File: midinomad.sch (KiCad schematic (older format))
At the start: 47 parts, among them U1 6N138

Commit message: Updated schematics. Still work in progress.
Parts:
- removed D2, D3: 1N4148, Diode_THT:D_DO-35_SOD27_P7.62mm_Horizontal, symbol Diode:1N4148
- removed R4: 4k7, symbol Device:R
- removed R5: 470R, symbol Device:R
- removed R6: 10k, symbol Device:R
- removed R7: 8k2, symbol Device:R
- removed R8: 300R, symbol Device:R
- added C1: 0.33uF, symbol pspice:C
- added C2: 0.1uF, symbol pspice:C
- added J2: MIDI OUT, w_conn_av:din-5, symbol Connector:DIN-5_180degree
- added J5: Conn_01x10_Female, symbol Connector:Conn_01x10_Female
- added J6: Conn_01x10_Male, symbol Connector:Conn_01x10_Male
- added J7: Jack-DC, symbol Connector:Jack-DC
- added JP2: Jumper, Connector_PinHeader_2.54mm:PinHeader_1x02_P2.54mm_Vertical, symbol Device:Jumper
- added R16: 9k1, Resistor_THT:R_Axial_DIN0207_L6.3mm_D2.5mm_P10.16mm_Horizontal, symbol Device:R
- added R17: 5k6, Resistor_THT:R_Axial_DIN0207_L6.3mm_D2.5mm_P10.16mm_Horizontal, symbol Device:R
- added R18: 2k7, Resistor_THT:R_Axial_DIN0207_L6.3mm_D2.5mm_P10.16mm_Horizontal, symbol Device:R
- added R25: 220R, Resistor_THT:R_Axial_DIN0207_L6.3mm_D2.5mm_P10.16mm_Horizontal, symbol Device:R
- added U2: L7805, symbol Regulator_Linear:L7805
- D2, D3, D4, D5, D6, D7: renamed from D?; footprint (none) -> LED_THT:LED_D5.0mm
- J1: renamed from J?; value DIN-5_180degree -> MIDI IN; footprint (none) -> w_conn_av:din-5
- J3: renamed from J?; footprint (none) -> w_conn_av:din-5; Note (none) -> Nomad 45, 55
- J4: renamed from J?; footprint (none) -> Connector_PinHeader_2.54mm:PinHeader_1x07_P2.54mm_Vertical; Note (none) -> Nomad 100
- JP1: renamed from JP?; footprint (none) -> Connector_PinHeader_2.54mm:PinHeader_1x02_P2.54mm_Vertical
- R1, R2, R3: footprint (none) -> Resistor_THT:R_Axial_DIN0207_L6.3mm_D2.5mm_P10.16mm_Horizontal
- R10, R11, R12, R13, R14, R15, R19, R20, R21, R22, R23, R24, R4, R5, R6, R7, R8, R9: renamed from R?; footprint (none) -> Resistor_THT:R_Axial_DIN0207_L6.3mm_D2.5mm_P10.16mm_Horizontal
- SW1, SW2, SW3, SW4, SW5, SW6: renamed from SW?; footprint (none) -> Button_Switch_THT:SW_PUSH_6mm
- U1: footprint (none) -> Package_DIP:DIP-8_W7.62mm
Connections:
- net +2V: now also J4.2, R16.2
- net +5V: now also A1.30 (VIN), C2.1, J6.1 (Pin_1), R25.1, U2.3 (OUT); no longer A1.27 (+5V)
- net -3V: now also J4.1, J6.8 (Pin_8), R17.1
- net Arduino_D2: now also J6.2 (Pin_2)
- net Arduino_D3: now also J6.3 (Pin_3)
- net Arduino_D4: now also J4.5
- net Arduino_D5: now also J4.4
- net Arduino_D6: now also J4.6
- net GNDREF: now also C1.2, C2.2, J2.2, J6.10 (Pin_10), J7.2, U2.2 (GND)
- net MESA_VCH: now also J4.3, J6.4 (Pin_4)
- net at A1.1 (D1/TX): now also JP2.2
- new net: J6.6 (Pin_6), R16.1, R17.2, R18.2
- new net: J6.7 (Pin_7), R18.1
- new net: C1.1, J7.1, U2.1 (IN)
- new net: J2.4, R25.2
- new net Relay_COM1: J5.4 (Pin_4)
- new net Relay_COM2: J5.7 (Pin_7)
- new net Relay_GND: J5.10 (Pin_10)
- new net Relay_In1: J5.2 (Pin_2)
- new net Relay_In2: J5.3 (Pin_3)
- new net Relay_NC1: J5.5 (Pin_5)
- new net Relay_NC2: J5.8 (Pin_8)
- new net Relay_NO1: J5.6 (Pin_6)
- new net Relay_NO2: J5.9 (Pin_9)
- new net Relay_Ucc: J5.1 (Pin_1)
- new net Tx: J2.5, JP2.1
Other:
- moved on the sheet: A1, D1, D2, D3, D4, D5, D6, D7, J1, J3, J4, JP1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

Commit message: Schematics update, arduino code finished.
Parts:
- removed J5: Conn_01x10_Female, symbol Connector:Conn_01x10_Female
- removed J6: Conn_01x10_Male, symbol Connector:Conn_01x10_Male
- added J5: Conn_01x04_Female, symbol Connector:Conn_01x04_Female
- added J6: Conn_01x06_Female, symbol Connector:Conn_01x06_Female
- added J8: Conn_01x04_Male, symbol Connector:Conn_01x04_Male
- added J9: Conn_01x06_Male, symbol Connector:Conn_01x06_Male
- added R26: 9k1, Resistor_THT:R_Axial_DIN0207_L6.3mm_D2.5mm_P10.16mm_Horizontal, symbol Device:R
- added R27: 5k6, Resistor_THT:R_Axial_DIN0207_L6.3mm_D2.5mm_P10.16mm_Horizontal, symbol Device:R
- added R28: 2k7, Resistor_THT:R_Axial_DIN0207_L6.3mm_D2.5mm_P10.16mm_Horizontal, symbol Device:R
- added Relay1, Relay2: SW_SPDT, symbol Switch:SW_SPDT
- U2: footprint (none) -> Package_TO_SOT_THT:TO-220-3_Vertical
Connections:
- net +2V: now also R26.2
- net +5V: now also J8.1 (Pin_1)
- net -3V: now also J9.5 (Pin_5), R27.1, Relay2.2 (B)
- net Arduino_D2: now also J8.2 (Pin_2)
- net Arduino_D3: now also J8.3 (Pin_3)
- net GNDREF: now also J8.4 (Pin_4)
- net MESA_VCH: now also J9.1 (Pin_1), Relay1.2 (B)
- net Relay_COM1: now also J6.1 (Pin_1)
- net Relay_COM2: now also J6.4 (Pin_4)
- net Relay_GND: now also J5.4 (Pin_4)
- net Relay_In1: now also J5.2 (Pin_2)
- net Relay_In2: now also J5.3 (Pin_3)
- net Relay_NC1: now also J6.2 (Pin_2)
- net Relay_NC2: now also J6.5 (Pin_5)
- net Relay_NO1: now also J6.3 (Pin_3)
- net Relay_NO2: now also J6.6 (Pin_6)
- net Relay_Ucc: now also J5.1 (Pin_1)
- net at R16.1, R17.2, R18.2: now also J9.3 (Pin_3)
- net at R18.1: now also J9.4 (Pin_4)
- new net: R26.1, R27.2, R28.2, Relay1.3 (C)
- new net: R28.1, Relay2.3 (C)
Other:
- moved on the sheet: A1, JP1, JP2, R19, R20, R21, R22, R23, R24, SW1, SW2, SW3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

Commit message: schematics related changes
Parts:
- J7: footprint (none) -> Connector_BarrelJack:BarrelJack_Horizontal
- J8: footprint (none) -> Connector_PinHeader_2.54mm:PinHeader_1x04_P2.54mm_Vertical
- J9: footprint (none) -> Connector_PinHeader_2.54mm:PinHeader_1x06_P2.54mm_Vertical
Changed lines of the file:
@@
 F 0 "J7" H 1107 3925 50  0000 C CNN
 F 1 "Jack-DC" H 1107 3834 50  0000 C CNN
-F 2 "" H 1100 3560 50  0001 C CNN
+F 2 "Connector_BarrelJack:BarrelJack_Horizontal" H 1100 3560 50  0001 C CNN
 F 3 "~" H 1100 3560 50  0001 C CNN
 	1    1050 3600
@@
 F 0 "J8" H 9108 2581 50  0000 C CNN
 F 1 "Conn_01x04_Male" H 9108 2490 50  0000 C CNN
-F 2 "" H 9000 2300 50  0001 C CNN
+F 2 "Connector_PinHeader_2.54mm:PinHeader_1x04_P2.54mm_Vertical" H 9000 2300 50  0001 C CNN
 F 3 "~" H 9000 2300 50  0001 C CNN
 	1    9000 2300
@@
 F 0 "J9" H 9108 3381 50  0000 C CNN
 F 1 "Conn_01x06_Male" H 9108 3290 50  0000 C CNN
-F 2 "" H 9000 3000 50  0001 C CNN
+F 2 "Connector_PinHeader_2.54mm:PinHeader_1x06_P2.54mm_Vertical" H 9000 3000 50  0001 C CNN
 F 3 "~" H 9000 3000 50  0001 C CNN
 	1    9000 3000

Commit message: schematics updated, using analog mux for vch switching, PCB nearly done
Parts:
- removed J5: Conn_01x04_Female, symbol Connector:Conn_01x04_Female
- removed J6: Conn_01x06_Female, symbol Connector:Conn_01x06_Female
- removed J8: Conn_01x04_Male, Connector_PinHeader_2.54mm:PinHeader_1x04_P2.54mm_Vertical, symbol Connector:Conn_01x04_Male
- removed J9: Conn_01x06_Male, Connector_PinHeader_2.54mm:PinHeader_1x06_P2.54mm_Vertical, symbol Connector:Conn_01x06_Male
- added H1, H2, H3, H4: MountingHole_Pad, MountingHole:MountingHole_3.2mm_M3_DIN965_Pad, symbol Mechanical:MountingHole_Pad
- added U3: 74HC4053, Package_DIP:DIP-16_W7.62mm_LongPads, symbol 74xx:74HC4053
- C1, C2: footprint (none) -> Capacitor_THT:C_Disc_D6.0mm_W2.5mm_P5.00mm
- J3: value DIN-5_180degree -> Nomad 5pin
- J4: value DIN-8 -> Nomad 100; symbol Connector:DIN-8 -> Connector:DIN-7; Note Nomad 100 -> (none)
- J7: value Jack-DC -> DC IN
- U2: footprint Package_TO_SOT_THT:TO-220-3_Vertical -> Package_TO_SOT_THT:TO-220-3_Horizontal_TabDown
- renumbered SW1 to CH1, SW2 to CH2, SW3 to CH3, SW6 to EQ1, Relay1 to MuxA1, Relay2 to MuxB1, SW5 to REV1, SW4 to SOLO1
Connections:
- net +5V: now also U3.16 (VCC)
- net -3V: now also U3.15 (BO)
- net Arduino_D2: now also U3.11 (A)
- net Arduino_D3: now also U3.10 (B)
- net GNDREF: now also H1.1, H2.1, H3.1, H4.1, U3.6 (INH), U3.7 (VEE), U3.8 (GND)
- net MESA_VCH: now also U3.14 (AO)
- net at R16.1, R17.2, R18.2: now also U3.13 (AY)
- net at R18.1: now also U3.1 (BY)
- no-connect marks 14 -> 20
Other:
- moved on the sheet: C1, C2, J7, R16, R17, R18, U2

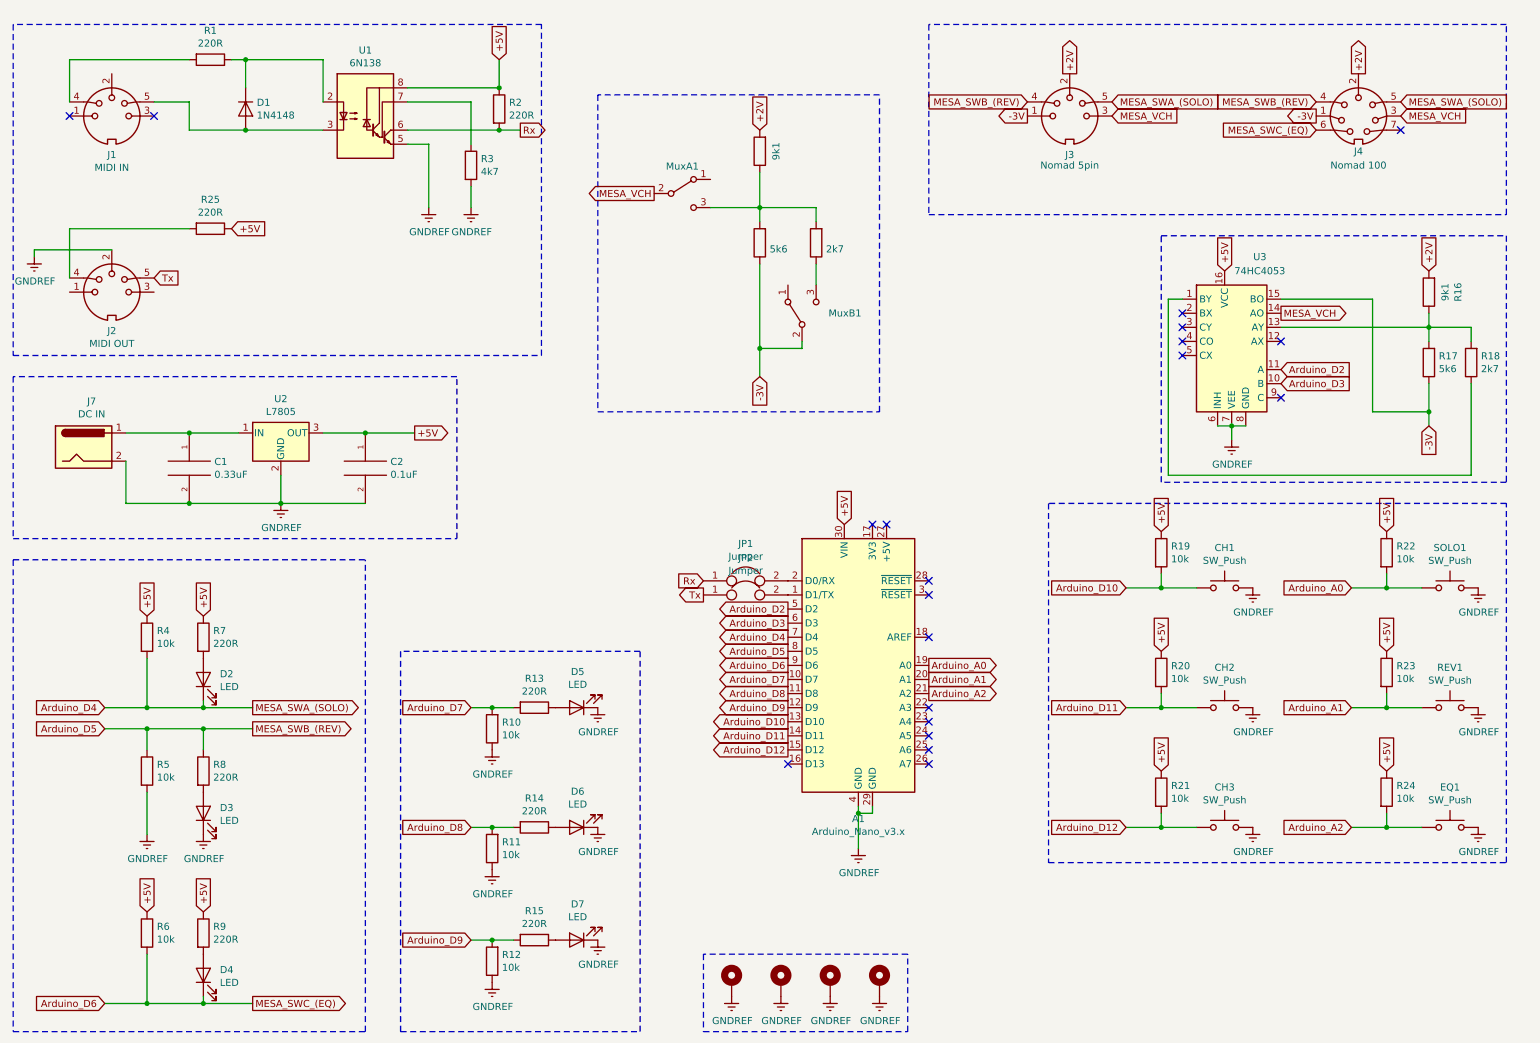
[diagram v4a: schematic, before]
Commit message: Updated both schematics & PCB, added second 74hc4053.
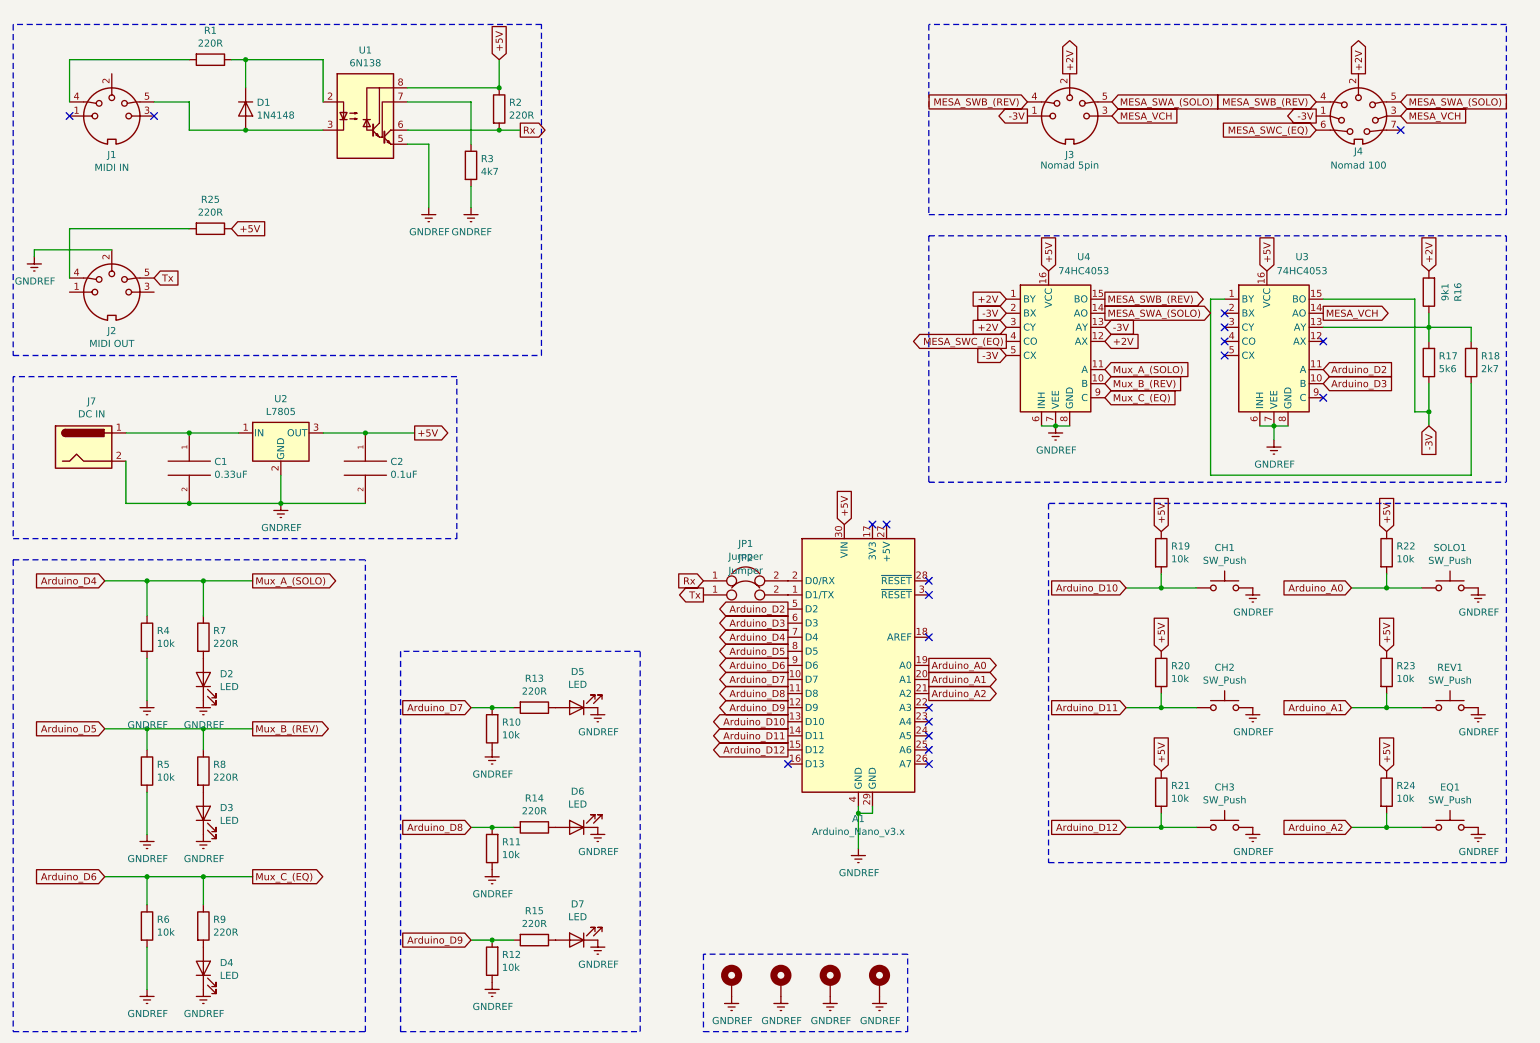
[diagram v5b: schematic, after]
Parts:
- removed MuxA1, MuxB1: SW_SPDT, symbol Switch:SW_SPDT
- removed R26: 9k1, Resistor_THT:R_Axial_DIN0207_L6.3mm_D2.5mm_P10.16mm_Horizontal, symbol Device:R
- removed R27: 5k6, Resistor_THT:R_Axial_DIN0207_L6.3mm_D2.5mm_P10.16mm_Horizontal, symbol Device:R
- removed R28: 2k7, Resistor_THT:R_Axial_DIN0207_L6.3mm_D2.5mm_P10.16mm_Horizontal, symbol Device:R
- added U4: 74HC4053, Package_DIP:DIP-16_W7.62mm_LongPads, symbol 74xx:74HC4053
- J4: footprint Connector_PinHeader_2.54mm:PinHeader_1x07_P2.54mm_Vertical -> midinomad:din-8
- U2: footprint Package_TO_SOT_THT:TO-220-3_Horizontal_TabDown -> Package_TO_SOT_THT:TO-220-3_Vertical
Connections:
- net +2V: now also U4.1 (BY), U4.12 (AX), U4.3 (CY)
- net +5V: now also U4.16 (VCC); no longer R4.1, R6.1, R7.1, R9.1
- net -3V: now also U4.13 (AY), U4.2 (BX), U4.5 (CX)
- net Arduino_D4: now also R4.1, R7.1, U4.11 (A); no longer D2.1 (K), J3.5, J4.5, R4.2
- net Arduino_D5: now also U4.10 (B); no longer J3.4, J4.4
- net Arduino_D6: now also R6.1, R9.1, U4.9 (C); no longer D4.1 (K), J4.6, R6.2
- net GNDREF: now also D2.1 (K), D4.1 (K), R4.2, R6.2, U4.6 (INH), U4.7 (VEE), U4.8 (GND)
- new net MESA_SWA_(SOLO): J3.5, J4.5, U4.14 (AO)
- new net MESA_SWB_(REV): J3.4, J4.4, U4.15 (BO)
- new net MESA_SWC_(EQ): J4.6, U4.4 (CO)
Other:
- moved on the sheet: D4, R6, R9, U3
